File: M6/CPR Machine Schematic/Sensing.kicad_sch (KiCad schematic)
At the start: 14 parts, among them J6 I2C Port, J9 Force Sensor, U4 MCP6004, U5 MCP3021A5T-E_OT

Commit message: BoM Fixes
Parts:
- C7: digikey 1292-1206N470J102CT-ND -> 732-7874-1-ND
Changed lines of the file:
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@@
 			)
 		)
-		(property "Datasheet" "http://www.passivecomponent.com/wp-content/uploads/datasheet/WTC_MLCC_Middle_and_High_Voltage.pdf"
+		(property "Datasheet" "https://www.digikey.com/en/products/detail/w%C3%BCrth-elektronik/885012008021/5453729"
 			(at 53.34 67.31 0)
 			(effects
@@
 			)
 		)
-		(property "digikey" "1292-1206N470J102CT-ND"
+		(property "digikey" "732-7874-1-ND"
 			(at 53.34 67.31 90)
 			(effects
@@
 			)
 		)
-		(property "Value" "47 pF"
-			(at 71.882 49.53 0)
-			(effects
-				(font
-					(size 1.27 1.27)
-				)
+		(property "Value" "+3V3"
+			(at 36.83 36.8299 0)
+			(effects
+				(font
+					(size 1.27 1.27)
+				)
+				(justify left)
 			)
 		)
@@
 				)
 				(hide yes)
-			)
-		)
-		(property "Value" "+3V3"
-			(at 36.83 36.8299 0)
-			(effects
-				(font
-					(size 1.27 1.27)
-				)
-				(justify left)
 			)
 		)
@@
 			)
 		)
-		(property "Value" "0.1 uF"
-			(at 127.762 41.91 0)
-			(effects
-				(font
-					(size 1.27 1.27)
-				)
+		(property "Value" "+3V3"
+			(at 59.69 39.3699 0)
+			(effects
+				(font
+					(size 1.27 1.27)
+				)
+				(justify left)
 			)
 		)
@@
 			)
 		)
-		(property "Value" "+3V3"
-			(at 59.69 39.3699 0)
-			(effects
-				(font
-					(size 1.27 1.27)
-				)
-				(justify left)
-			)
-		)

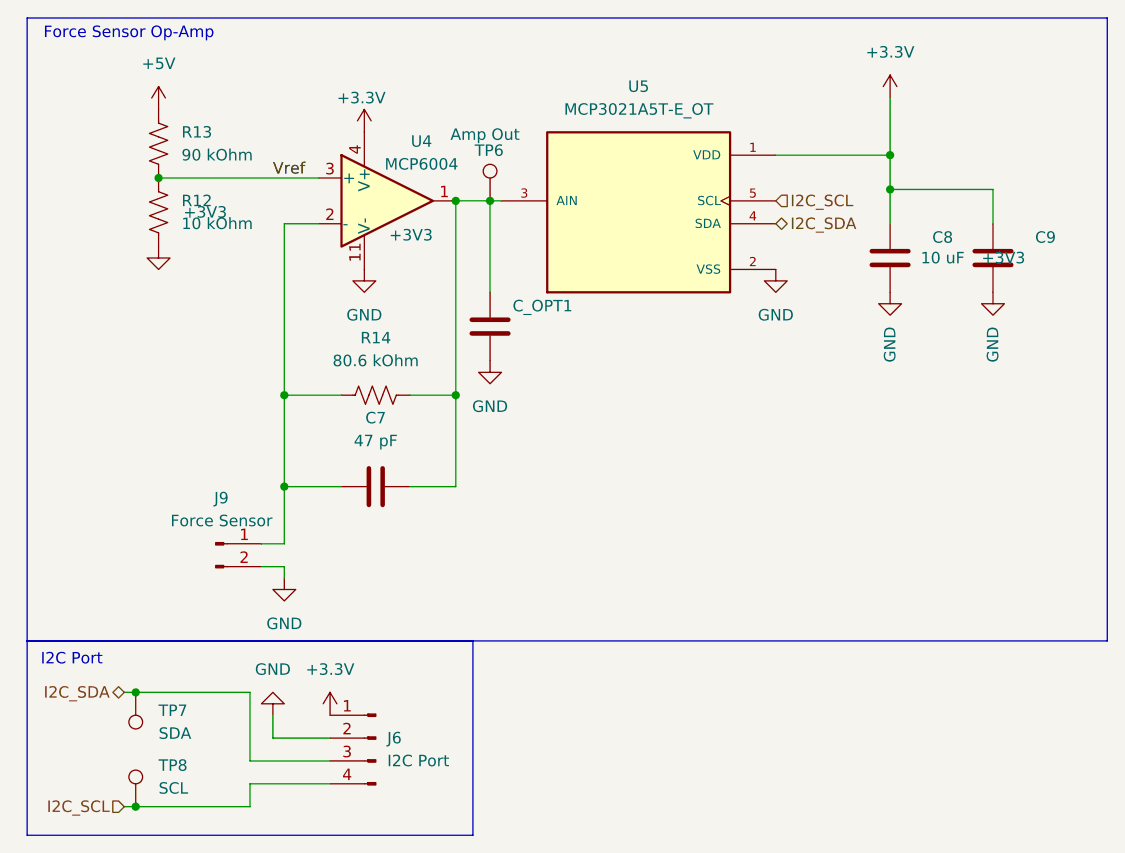
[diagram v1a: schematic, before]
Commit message: Missing cap values
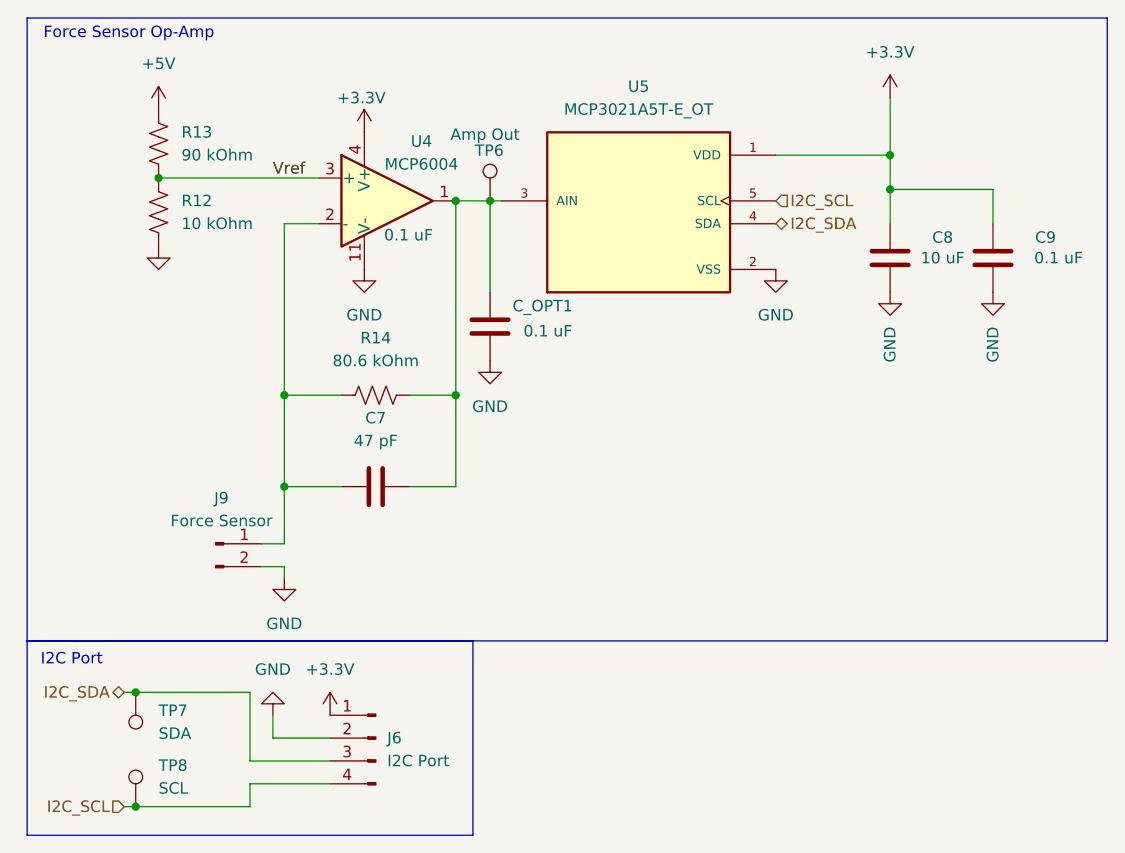
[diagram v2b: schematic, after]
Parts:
- C9, C_OPT1: value +3V3 -> 0.1 uF
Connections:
- net +3V3 renamed 0.1 uF
